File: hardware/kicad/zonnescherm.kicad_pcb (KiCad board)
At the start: 2 copper layers, 24 parts, among them K1 K1-ON/OFF, K2 K1-UP/DOWN, K3 K2-ON/OFF, K4 K2-UP/DOWN, P1 ARDUINO-ISP, SW1 SW_UP_1, SW2 SW_DOWN_1, SW3 SW_UP_2, SW4 SW_DOWN_2, U2 LM1117-3.3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

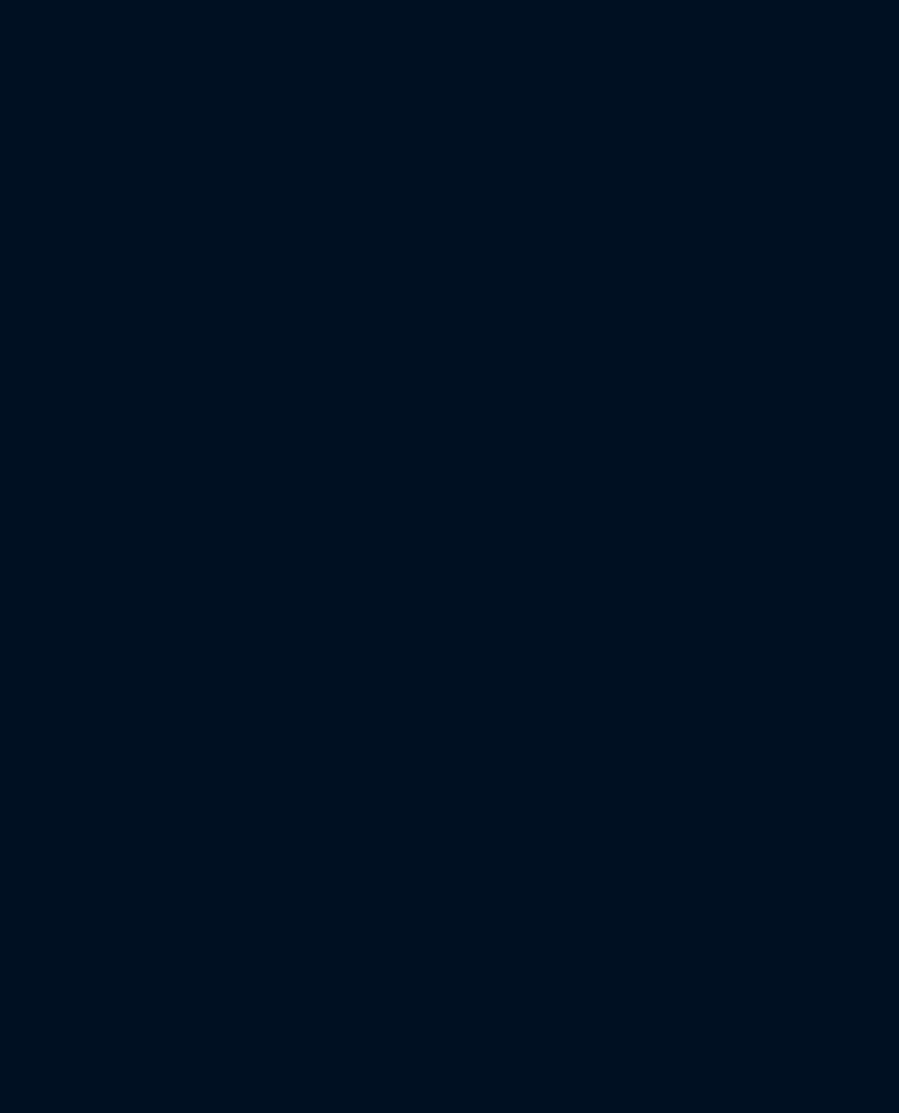
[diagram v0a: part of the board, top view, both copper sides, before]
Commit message: Added AKL-330-4 footprint
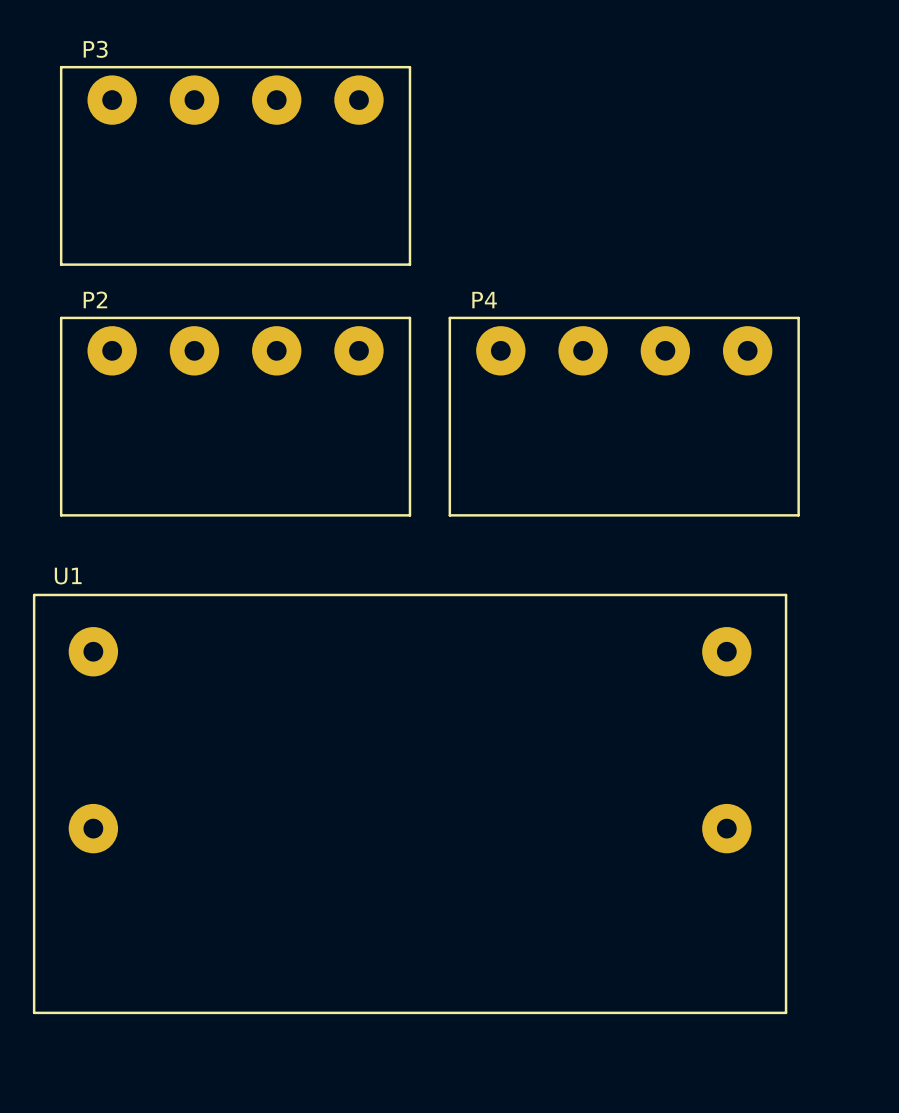
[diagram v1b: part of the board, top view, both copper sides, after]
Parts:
- added P2: CONN_MAINS, modex:AKL-330-4, F.Cu at (50.5, 92.7)
- added P3: CONN_SUNSHADE1, modex:AKL-330-4, F.Cu at (50.5, 77.5)
- added P4: CONN_SUNSHADE2, modex:AKL-330-4, F.Cu at (74.2, 92.7)
- added U1: IRM-05-5, modex:IRM-05, F.Cu at (49.4, 111.0)
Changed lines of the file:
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@@
 (kicad_pcb (version 4) (host pcbnew 4.0.2+e4-6225~38~ubuntu14.04.1-stable)
   (general
-    (links 53)
-    (no_connects 53)
+    (links 62)
+    (no_connects 62)
     (area 0 0 0 0)
     (thickness 1.6)
@@
     (tracks 0)
     (zones 0)
-    (modules 24)
-    (nets 36)
+    (modules 28)
+    (nets 43)
   )
   (page A4)
@@
   (net 34 "Net-(U4-Pad10)")
   (net 35 "Net-(K2-Pad1)")
+  (net 36 PE)
+  (net 37 N)
+  (net 38 "Net-(P2-Pad2)")
+  (net 39 "Net-(K2-Pad5)")
+  (net 40 "Net-(K2-Pad3)")
+  (net 41 "Net-(K4-Pad5)")
+  (net 42 "Net-(K4-Pad3)")
   (net_class Default "This is the default net class."
     (clearance 0.2)
@@
     (add_net GPIO4)
     (add_net GPIO5)
+    (add_net N)
     (add_net "Net-(F1-Pad2)")
     (add_net "Net-(K1-Pad1)")
     (add_net "Net-(K2-Pad1)")
+    (add_net "Net-(K2-Pad3)")
+    (add_net "Net-(K2-Pad5)")
     (add_net "Net-(K3-Pad1)")
     (add_net "Net-(K4-Pad1)")
+    (add_net "Net-(K4-Pad3)")
+    (add_net "Net-(K4-Pad5)")
     (add_net "Net-(P1-Pad1)")
     (add_net "Net-(P1-Pad4)")
     (add_net "Net-(P1-Pad5)")
+    (add_net "Net-(P2-Pad2)")
     (add_net "Net-(U3-Pad10)")
     (add_net "Net-(U3-Pad11)")
@@
     (add_net P3V3)
     (add_net P5V)
+    (add_net PE)
     (add_net RXD)
     (add_net TXD)
@@
       (rotate (xyz 0 0 0))
     )
+  )
+  (module modex:AKL-330-4 (layer F.Cu)
+    (at 50.546 92.71)
+    (descr "Fujitsu Relay")
+    (fp_text reference P2 (at -1.016 -3.048) (layer F.SilkS)
+      (effects (font (size 1 1) (thickness 0.15)))
+    )
+    (fp_text value CONN_MAINS (at 7.62 11.684) (layer F.Fab)
+      (effects (font (size 1 1) (thickness 0.15)))
+    )
+    (fp_line (start 18.1 -2) (end 18.1 10) (layer F.SilkS) (width 0.15))
+    (fp_line (start 18.1 10) (end -3.1 10) (layer F.SilkS) (width 0.15))
+    (fp_line (start -3.1 10) (end -3.1 -2) (layer F.SilkS) (width 0.15))
+    (fp_line (start -3.1 -2) (end 18.1 -2) (layer F.SilkS) (width 0.15))
+    (pad 4 thru_hole circle (at 15 0 180) (size 3 3) (drill 1.2) (layers *.Cu *.Mask F.SilkS)
+      (net 36 PE))
+    (pad 3 thru_hole circle (at 10 0 180) (size 3 3) (drill 1.2) (layers *.Cu *.Mask F.SilkS)
+      (net 37 N))
+    (pad 2 thru_hole circle (at 5 0 180) (size 3 3) (drill 1.2) (layers *.Cu *.Mask F.SilkS)
+      (net 38 "Net-(P2-Pad2)"))
+    (pad 1 thru_hole circle (at 0 0 180) (size 3 3) (drill 1.2) (layers *.Cu *.Mask F.SilkS)
+      (net 5 "Net-(F1-Pad2)"))
+    (model Relays_ThroughHole.3dshapes/Relay_SPDT_SingleRow_Standing_FinderType34Point51.wrl
+      (at (xyz 0 0 0))
+      (scale (xyz 1 1 1))
+      (rotate (xyz 0 0 0))
+    )
+  )
+  (module modex:AKL-330-4 (layer F.Cu)
+    (at 50.546 77.47)
+    (descr "Fujitsu Relay")
+    (fp_text reference P3 (at -1.016 -3.048) (layer F.SilkS)
+      (effects (font (size 1 1) (thickness 0.15)))
+    )
+    (fp_text value CONN_SUNSHADE1 (at 7.62 11.684) (layer F.Fab)
+      (effects (font (size 1 1) (thickness 0.15)))
+    )
+    (fp_line (start 18.1 -2) (end 18.1 10) (layer F.SilkS) (width 0.15))
+    (fp_line (start 18.1 10) (end -3.1 10) (layer F.SilkS) (width 0.15))
+    (fp_line (start -3.1 10) (end -3.1 -2) (layer F.SilkS) (width 0.15))
+    (fp_line (start -3.1 -2) (end 18.1 -2) (layer F.SilkS) (width 0.15))
+    (pad 4 thru_hole circle (at 15 0 180) (size 3 3) (drill 1.2) (layers *.Cu *.Mask F.SilkS)
+      (net 36 PE))
+    (pad 3 thru_hole circle (at 10 0 180) (size 3 3) (drill 1.2) (layers *.Cu *.Mask F.SilkS)
+      (net 37 N))
+    (pad 2 thru_hole circle (at 5 0 180) (size 3 3) (drill 1.2) (layers *.Cu *.Mask F.SilkS)
+      (net 39 "Net-(K2-Pad5)"))
+    (pad 1 thru_hole circle (at 0 0 180) (size 3 3) (drill 1.2) (layers *.Cu *.Mask F.SilkS)
+      (net 40 "Net-(K2-Pad3)"))
+    (model Relays_ThroughHole.3dshapes/Relay_SPDT_SingleRow_Standing_FinderType34Point51.wrl
+      (at (xyz 0 0 0))
+      (scale (xyz 1 1 1))
+      (rotate (xyz 0 0 0))
+    )
+  )
+  (module modex:AKL-330-4 (layer F.Cu)
+    (at 74.168 92.71)
+    (descr "Fujitsu Relay")
+    (fp_text reference P4 (at -1.016 -3.048) (layer F.SilkS)
+      (effects (font (size 1 1) (thickness 0.15)))
+    )
+    (fp_text value CONN_SUNSHADE2 (at 7.62 11.684) (layer F.Fab)
+      (effects (font (size 1 1) (thickness 0.15)))
+    )
+    (fp_line (start 18.1 -2) (end 18.1 10) (layer F.SilkS) (width 0.15))
+    (fp_line (start 18.1 10) (end -3.1 10) (layer F.SilkS) (width 0.15))
+    (fp_line (start -3.1 10) (end -3.1 -2) (layer F.SilkS) (width 0.15))
+    (fp_line (start -3.1 -2) (end 18.1 -2) (layer F.SilkS) (width 0.15))
+    (pad 4 thru_hole circle (at 15 0 180) (size 3 3) (drill 1.2) (layers *.Cu *.Mask F.SilkS)
+      (net 36 PE))
+    (pad 3 thru_hole circle (at 10 0 180) (size 3 3) (drill 1.2) (layers *.Cu *.Mask F.SilkS)
+      (net 37 N))
+    (pad 2 thru_hole circle (at 5 0 180) (size 3 3) (drill 1.2) (layers *.Cu *.Mask F.SilkS)
+      (net 41 "Net-(K4-Pad5)"))
+    (pad 1 thru_hole circle (at 0 0 180) (size 3 3) (drill 1.2) (layers *.Cu *.Mask F.SilkS)
+      (net 42 "Net-(K4-Pad3)"))
+    (model Relays_ThroughHole.3dshapes/Relay_SPDT_SingleRow_Standing_FinderType34Point51.wrl
+      (at (xyz 0 0 0))
+      (scale (xyz 1 1 1))
+      (rotate (xyz 0 0 0))
+    )
+  )
+  (module modex:IRM-05 (layer F.Cu)
+    (at 49.403 110.998)
+    (descr "Fujitsu Relay")
+    (fp_text reference U1 (at -1.524 -4.572) (layer F.SilkS)
+      (effects (font (size 1 1) (thickness 0.15)))
+    )
+    (fp_text value IRM-05-5 (at 21.336 23.876) (layer F.Fab)
+      (effects (font (size 1 1) (thickness 0.15)))
+    )
+    (fp_line (start 42.1 21.95) (end 42.1 -3.45) (layer F.SilkS) (width 0.15))
+    (fp_line (start -3.6 21.95) (end 42.1 21.95) (layer F.SilkS) (width 0.15))
+    (fp_line (start -3.6 -3.45) (end -3.6 21.95) (layer F.SilkS) (width 0.15))
+    (fp_line (start -3.6 -3.45) (end 42.1 -3.45) (layer F.SilkS) (width 0.15))
+    (pad 4 thru_hole circle (at 38.5 10.75 180) (size 3 3) (drill 1.2) (layers *.Cu *.Mask F.SilkS)
+      (net 2 GND))
+    (pad 3 thru_hole circle (at 0 10.75 180) (size 3 3) (drill 1.2) (layers *.Cu *.Mask F.SilkS)
+      (net 1 P5V))
+    (pad 2 thru_hole circle (at 38.5 0 180) (size 3 3) (drill 1.2) (layers *.Cu *.Mask F.SilkS)
+      (net 37 N))
+    (pad 1 thru_hole circle (at 0 0 180) (size 3 3) (drill 1.2) (layers *.Cu *.Mask F.SilkS)
+      (net 6 P))
+    (model Relays_ThroughHole.3dshapes/Relay_SPDT_SingleRow_Standing_FinderType34Point51.wrl
+      (at (xyz 0 0 0))
+      (scale (xyz 1 1 1))
+      (rotate (xyz 0 0 0))
+    )

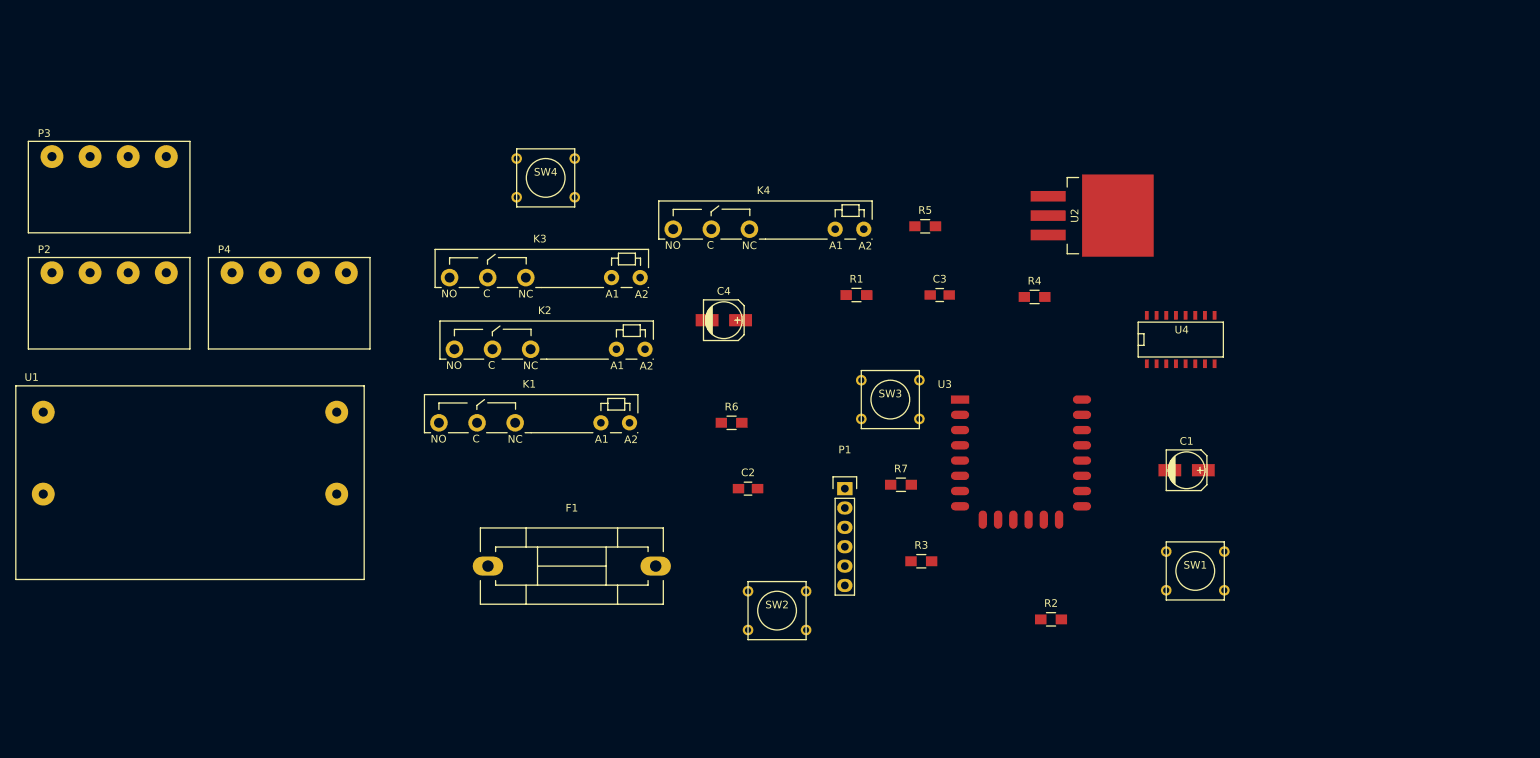
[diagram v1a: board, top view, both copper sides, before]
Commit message: Updated layout
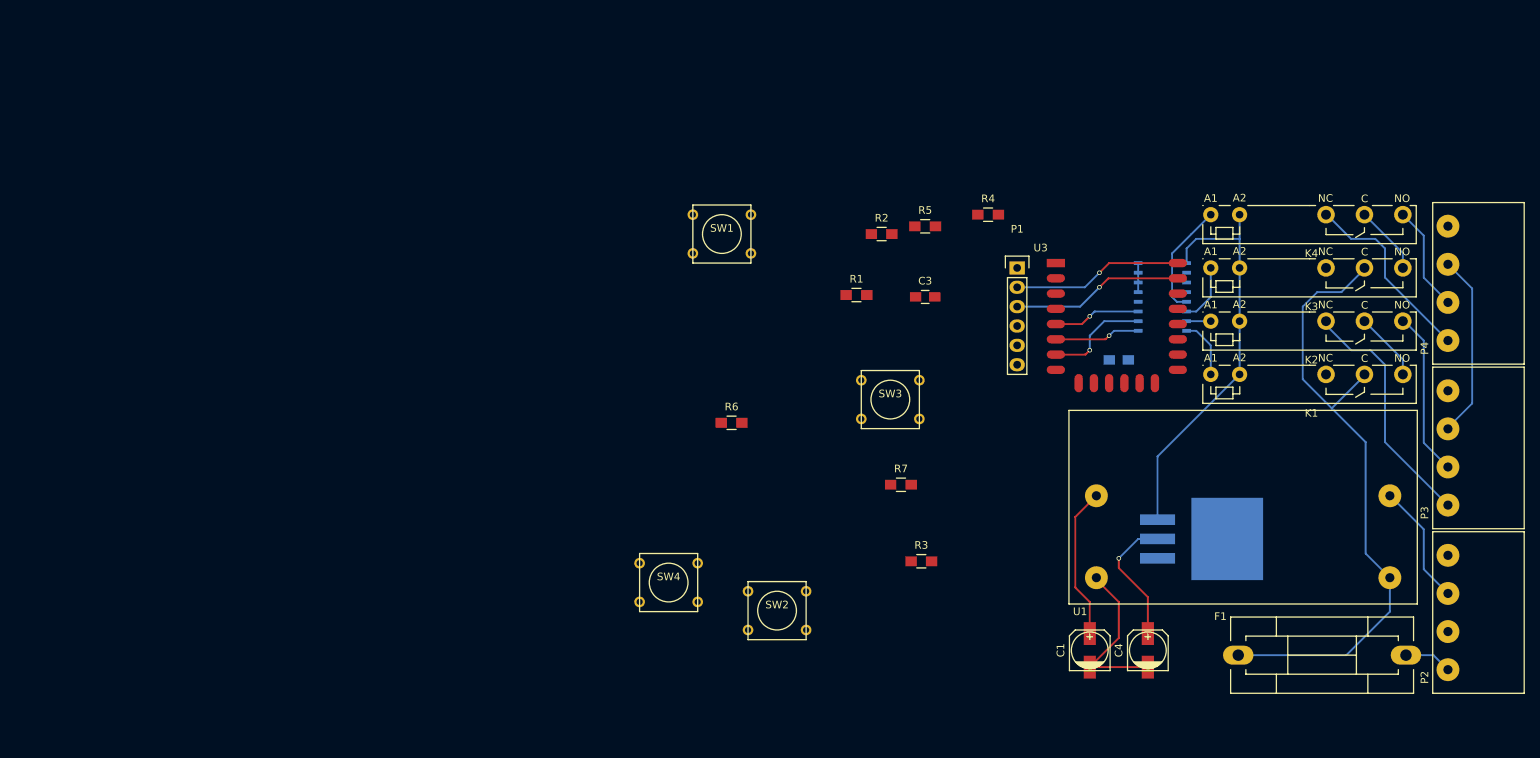
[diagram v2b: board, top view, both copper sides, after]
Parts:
- C2, U2, U4: moved to B.Cu
- moved P2 190.4 mm to (233.7, 144.8), turned to 90 degrees
- moved P3 188.8 mm to (233.7, 123.2), turned to 90 degrees
- moved U1 178.0 mm to (226.1, 132.7), turned to 180 degrees
- moved P4 159.8 mm to (233.7, 101.6), turned to 90 degrees
- moved F1 99.1 mm to (217.2, 142.9)
- moved K1 89.6 mm to (202.6, 106.0), turned to 180 degrees
- moved K3 88.0 mm to (202.6, 92.1), turned to 180 degrees
- moved K2 87.5 mm to (202.6, 99.1), turned to 180 degrees
- moved SW1 76.2 mm to (138.4, 87.6)
- moved C4 70.5 mm to (194.3, 142.2), turned to 90 degrees
- moved K4 58.7 mm to (202.6, 85.1), turned to 180 degrees
- moved SW4 55.5 mm to (131.4, 133.3)
- moved R2 55.2 mm to (159.4, 87.6)
- moved C2 51.5 mm to (190.5, 104.1)
- moved U2 44.8 mm to (195.6, 127.6)
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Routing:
- net P: track 0.00 -> 83.5 mm
- net P5V: track 0.00 -> 73.9 mm
- net N: track 0.00 -> 40.2 mm
- net Net-(K2-Pad3): track 0.00 -> 32.2 mm
- net GND: track 0.00 -> 26.0 mm
- net Net-(K4-Pad3): track 0.00 -> 25.1 mm
- net RXD: track 0.00 -> 22.6 mm, vias 0 -> 1
- net TXD: track 0.00 -> 22.4 mm, vias 0 -> 1
- net Net-(K2-Pad5): track 0.00 -> 21.7 mm
- net P3V3: track 0.00 -> 17.6 mm, vias 0 -> 1
- net Net-(K4-Pad1): track 0.00 -> 15.1 mm
- net Net-(K4-Pad5): track 0.00 -> 14.0 mm
- net Net-(U3-Pad7): track 0.00 -> 13.7 mm, vias 0 -> 1
- net Net-(U3-Pad5): track 0.00 -> 11.5 mm, vias 0 -> 1
- net Net-(U3-Pad6): track 0.00 -> 11.3 mm, vias 0 -> 1
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
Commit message: Updated PCB layout
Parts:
- C3, R1, R2, R3, R4, R5, R6, R7: moved to B.Cu
- moved SW1 56.8 mm to (172.5, 133.1), turned to 90 degrees
- moved SW4 42.1 mm to (172.2, 122.7), turned to 90 degrees
- moved SW3 41.7 mm to (167.0, 150.5)
- moved R7 39.1 mm to (200.2, 112.3), turned to 90 degrees
- moved R6 37.5 mm to (177.2, 112.4), turned to 90 degrees
- moved R1 34.9 mm to (186.7, 112.4), turned to 90 degrees
- moved R2 34.6 mm to (183.5, 112.4), turned to 90 degrees
- moved R4 33.7 mm to (193.0, 112.4), turned to 90 degrees
- moved R3 31.1 mm to (189.9, 112.4), turned to 90 degrees
- moved R5 29.9 mm to (180.3, 112.4), turned to 90 degrees
- moved C3 22.9 mm to (187.3, 90.2)
- moved U2 2.62 mm to (196.2, 130.2), turned to 90 degrees
- moved C4 1.91 mm to (196.2, 142.2)
- moved C2 1.37 mm to (190.0, 102.9)
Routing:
- net GND: track 26.0 -> 132.3 mm, vias 0 -> 2
- net PE: track 0.00 -> 54.8 mm
- net P3V3: track 17.6 -> 55.5 mm, vias 1 -> 2
- net GPIO15: track 0.00 -> 29.0 mm, vias 0 -> 3
- net XRES: track 0.00 -> 27.9 mm, vias 0 -> 2
- net N: track 40.2 -> 67.8 mm
- net GPIO5: track 0.00 -> 22.6 mm, vias 0 -> 1
- net GPIO4: track 0.00 -> 19.4 mm, vias 0 -> 1
- net EN: track 0.00 -> 17.2 mm, vias 0 -> 1
- net GPIO0: track 0.00 -> 16.1 mm, vias 0 -> 1
- net GPIO2: track 0.00 -> 12.9 mm, vias 0 -> 1
- net P5V: track 73.9 -> 81.6 mm, vias 0 -> 3
- net P: track 83.5 -> 80.9 mm
- net Net-(K4-Pad1): track 15.1 -> 13.1 mm
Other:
- net class Power added: clearance 0.2, trace_width 1, via_dia 0.6, via_drill 0.4
- board text added: "MODEX electronics"

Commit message: Updated PCB
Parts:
- removed SW1: SW_UP_1, Buttons_Switches_ThroughHole:SW_PUSH_SMALL
- removed SW2: SW_DOWN_1, Buttons_Switches_ThroughHole:SW_PUSH_SMALL
- removed SW3: SW_UP_2, Buttons_Switches_ThroughHole:SW_PUSH_SMALL
- removed SW4: SW_DOWN_2, Buttons_Switches_ThroughHole:SW_PUSH_SMALL
- added C5: 100n, Capacitors_SMD:C_0805_HandSoldering, B.Cu at (138.3, 99.6)
- added P5: CONN_02X04, Pin_Headers:Pin_Header_Straight_2x04, F.Cu at (109.0, 106.9)
- added REF**: MountingHole_3.2mm_M3, Mounting_Holes:MountingHole_3.2mm_M3, F.Cu at (109.5, 130.2)
- added REF**: MountingHole_3.2mm_M3, Mounting_Holes:MountingHole_3.2mm_M3, F.Cu at (108.6, 72.0)
- moved C2 69.4 mm to (121.9, 89.5)
- moved C1 69.2 mm to (118.6, 129.5)
- moved C4 69.2 mm to (128.1, 129.5)
- moved K1 69.2 mm to (134.5, 93.3)
- moved K2 69.2 mm to (134.5, 86.4)
- moved K3 69.2 mm to (134.5, 79.4)
- moved K4 69.2 mm to (134.5, 72.4)
- moved P2 69.2 mm to (165.6, 132.1)
- moved P3 69.2 mm to (165.6, 110.5)
- moved P4 69.2 mm to (165.6, 88.9)
- moved R1 69.2 mm to (118.6, 99.7)
- moved R3 69.2 mm to (121.8, 99.7)
- moved R5 69.2 mm to (112.3, 99.7)
- moved U1 69.2 mm to (158.0, 120.0)
- moved U2 69.2 mm to (128.1, 117.5)
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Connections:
- P2 pad 2: Net-(P2-Pad2) -> Net-(F1-Pad2)
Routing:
- net GND: track 132.3 -> 172.3 mm
- net GPIO2: track 12.9 -> 37.0 mm, vias 1 -> 2
- net P3V3: track 55.5 -> 78.6 mm
- net GPIO0: track 16.1 -> 35.8 mm, vias 1 -> 2
- net GPIO4: track 19.4 -> 36.7 mm, vias 1 -> 2
- net GPIO5: track 22.6 -> 36.2 mm, vias 1 -> 2
- net Net-(F1-Pad2): track 6.30 -> 11.3 mm
- net P5V: track 81.6 -> 85.9 mm, vias 3 -> 1
- net Net-(K4-Pad1): track 13.1 -> 14.5 mm
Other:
- board outline added: 74.9 x 80.9 mm

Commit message: Added logo
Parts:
- removed REF** (x2): MountingHole_3.2mm_M3, Mounting_Holes:MountingHole_3.2mm_M3
- added G***: LOGO, modex:modex, F.Cu at (139.2, 109.7)
- P5: value CONN_02X04 -> SWITCHES
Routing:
- net GND: track 172.3 -> 174.2 mm
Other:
- board size 74.9 x 80.9 mm -> 71.1 x 67.4 mm
- board text removed: "MODEX electronics"

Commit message: Updated layout, added text etc.
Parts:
- added REF**: board_75x75_mm, modex:board_75x75_mm_mod, F.Cu at (108.5, 58.9)
- C1: footprint Capacitors_SMD:c_elec_5x5.3 -> Capacitors_SMD:c_elec_8x6.5
- C4: footprint Capacitors_SMD:c_elec_5x5.3 -> Capacitors_SMD:c_elec_4x5.8
- moved G*** 20.6 mm to (132.8, 129.3)
- moved P2 10.1 mm to (173.2, 125.5)
- moved P3 10.1 mm to (173.2, 103.9)
- moved P4 10.1 mm to (173.2, 82.3)
- moved C4 9.20 mm to (131.3, 120.9)
- moved C1 8.49 mm to (115.4, 121.7), turned to 0 degrees
- moved F1 8.24 mm to (152.8, 122.8)
- moved C5 7.33 mm to (141.5, 93.0)
- moved K1 7.33 mm to (137.7, 86.7)
- moved K2 7.33 mm to (137.7, 79.8)
- moved K3 7.33 mm to (137.7, 72.8)
- moved K4 7.33 mm to (137.7, 65.8)
- moved P5 7.33 mm to (112.1, 100.3)
- moved R1 7.33 mm to (121.8, 93.1)
- moved U1 7.33 mm to (161.2, 113.4)
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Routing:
- net GND: track 174.2 -> 168.7 mm
- net Net-(F1-Pad2): track 11.3 -> 15.4 mm
- net Net-(K4-Pad3): track 25.0 -> 28.9 mm
- net N: track 67.8 -> 70.8 mm
- net P5V: track 85.9 -> 88.9 mm
- net Net-(K4-Pad5): track 14.0 -> 15.9 mm
- net Net-(K2-Pad5): track 21.7 -> 23.6 mm
- net Net-(K2-Pad3): track 32.2 -> 34.1 mm
- net P3V3: track 78.6 -> 77.0 mm
- net P: track 81.2 -> 80.3 mm
- net PE: track 54.8 -> 55.5 mm
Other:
- board size 71.1 x 67.4 mm -> 75 x 75 mm
- board text added: "L"
- board text added: "L1"
- board text added: "L2"
- board text added: "MAINS"
- board text added: "N"
- board text added: "PE"
- board text added: "SUNSHADE_1"
- board text added: "SUNSHADE_2"
